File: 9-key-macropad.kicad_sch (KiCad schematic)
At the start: 0 parts

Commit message: Controller and Switch Schematic Assignments
Added the Seeed Studio XIAO-RP2040-DIP module and generic push button switch symbols to the schematic. Updated project and schematic files to include symbol definitions, global labels for keys, and wiring for a 9-key macropad design.
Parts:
- added SW1, SW2, SW3, SW4, SW5, SW6, SW7, SW8, SW9: SW_Push, Button_Switch_Keyboard:SW_Cherry_MX_1.00u_Plate, symbol Switch:SW_Push
- added U1: XIAO-RP2040-DIP, Module:MOUDLE14P-XIAO-DIP-SMD, symbol Seeed_Studio_XIAO_Series:XIAO-RP2040-DIP
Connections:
- new net GNDD: SW1.2, SW2.2, SW3.2, SW4.2, SW5.2, SW6.2, SW7.2, SW8.2, SW9.2
- new net KEY1: SW1.1, U1.1 (GPIO26/ADC0/A0)
- new net KEY2: SW2.1, U1.2 (GPIO27/ADC1/A1)
- new net KEY3: SW3.1, U1.3 (GPIO28/ADC2/A2)
- new net KEY4: SW4.1, U1.4 (GPIO29/ADC3/A3)
- new net KEY5: SW5.1, U1.5 (GPIO6/SDA)
- new net KEY6: SW6.1, U1.6 (GPIO7/SCL)
- new net KEY7: SW7.1, U1.8 (GPIO1/RX)
- new net KEY8: SW8.1, U1.9 (GPIO2/SCK)
- new net KEY9: SW9.1, U1.10 (GPIO4/MISO)
- new net NEOPIX: U1.7 (GPIO0/TX)

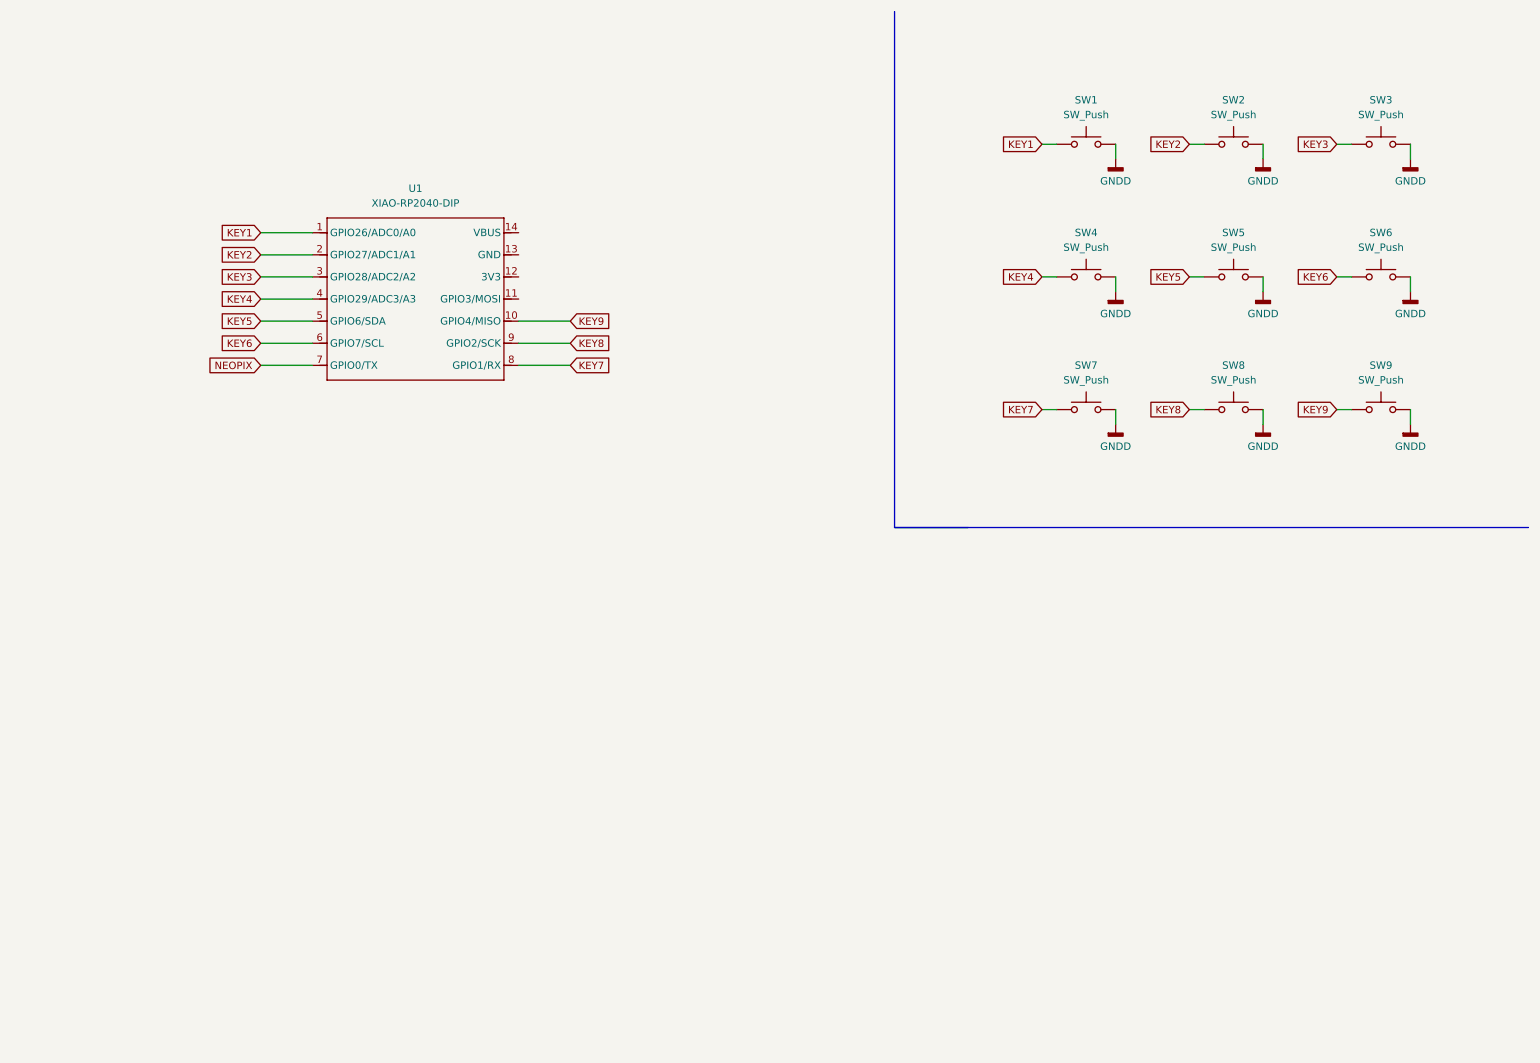
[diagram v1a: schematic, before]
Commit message: Add Step-Up library and update PCB + SCM
Added SN74AHCT1G125DBVR symbol, footprint, STEP model, and documentation to the libraries directory. Updated 9-key-macropad PCB, schematic, and project files to include new components and connections. Modified footprint and symbol library tables to reference the new library.
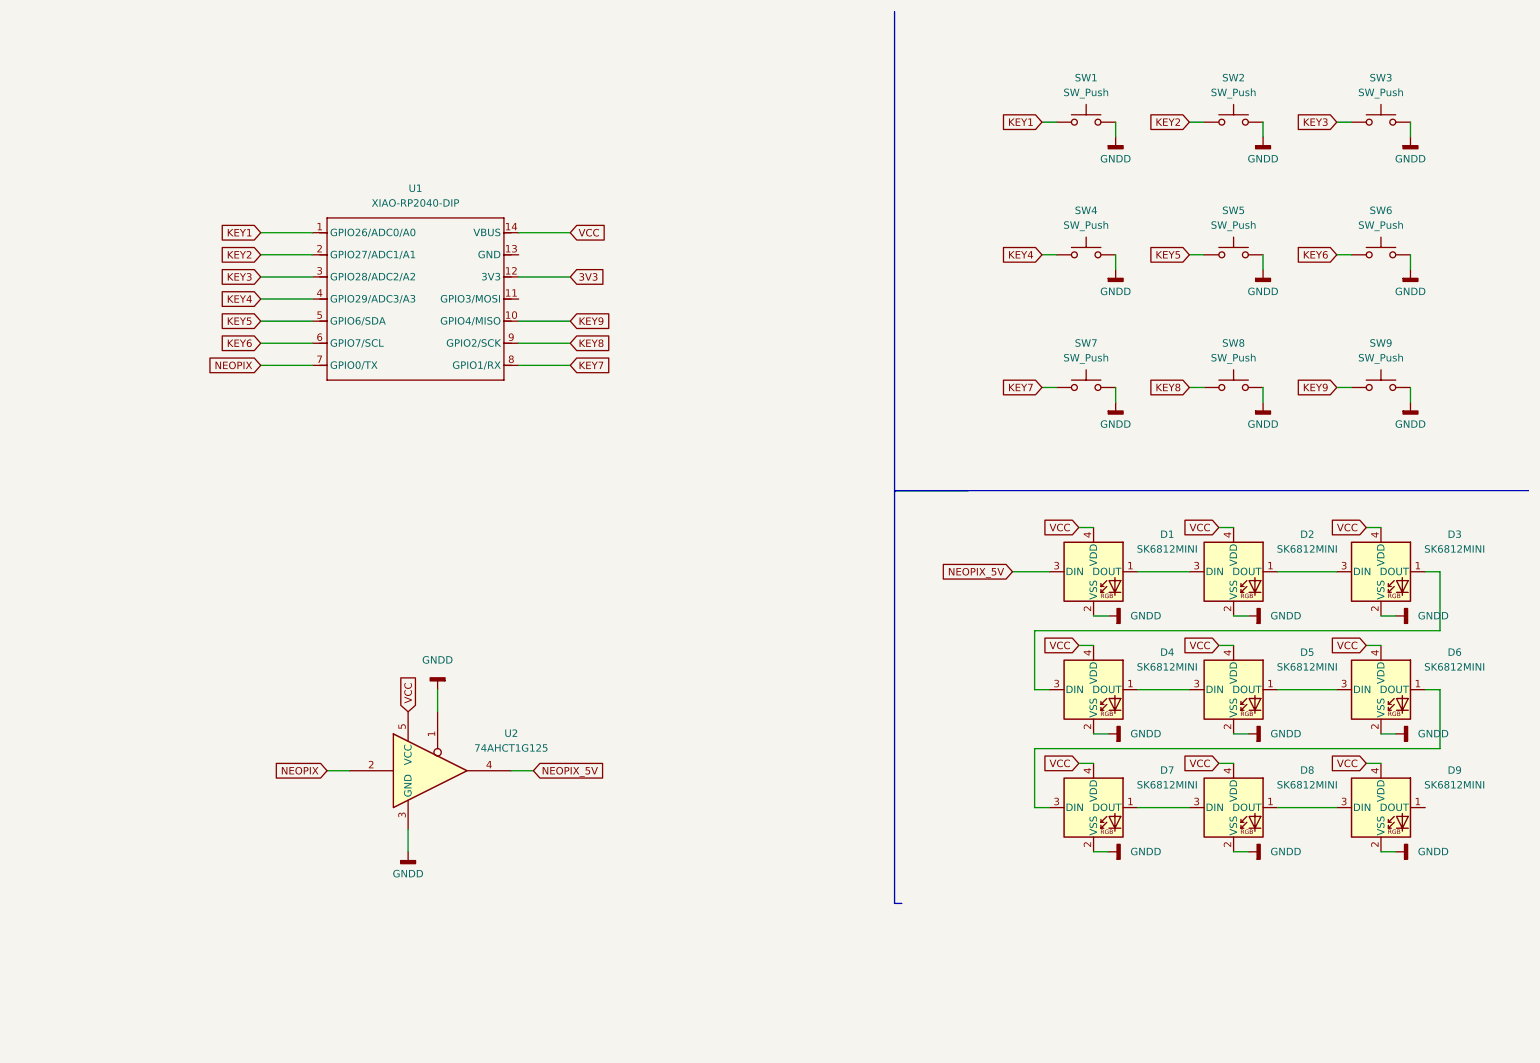
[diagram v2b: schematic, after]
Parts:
- added D1, D2, D3, D4, D5, D6, D7, D8, D9: SK6812MINI, LED_SMD:LED_SK6812MINI_PLCC4_3.5x3.5mm_P1.75mm, symbol LED:SK6812MINI
- added U2: 74AHCT1G125, SN74AHCT1G125DBVR:SOT95P280X145-5N, symbol 74xGxx:74AHCT1G125
- U1: footprint Module:MOUDLE14P-XIAO-DIP-SMD -> Seeed Studio XIAO Series Library:XIAO-RP2040-DIP
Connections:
- net GNDD: now also D1.2 (VSS), D2.2 (VSS), D3.2 (VSS), D4.2 (VSS), D5.2 (VSS), D6.2 (VSS), D7.2 (VSS), D8.2 (VSS), D9.2 (VSS), U2.1, U2.3 (GND)
- net NEOPIX: now also U2.2
- net 3V3: now reaches U1.12 (3V3)
- net VCC: now reaches U1.14 (VBUS)
- net VCC: now also D1.4 (VDD), D2.4 (VDD), D3.4 (VDD), D4.4 (VDD), D5.4 (VDD), D6.4 (VDD), D7.4 (VDD), D8.4 (VDD), D9.4 (VDD), U2.5 (VCC)
- new net: D6.1 (DOUT), D7.3 (DIN)
- new net: D5.1 (DOUT), D6.3 (DIN)
- new net: D8.1 (DOUT), D9.3 (DIN)
- new net: D7.1 (DOUT), D8.3 (DIN)
- new net: D4.1 (DOUT), D5.3 (DIN)
- new net: D3.1 (DOUT), D4.3 (DIN)
- new net: D2.1 (DOUT), D3.3 (DIN)
- new net: D1.1 (DOUT), D2.3 (DIN)
- new net NEOPIX_5V: D1.3 (DIN), U2.4
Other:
- moved on the sheet: SW1, SW2, SW3, SW4, SW5, SW6, SW7, SW8, SW9

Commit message: Rearrange key switches and LEDs, update net assignments
Moved key switches and SK6812MINI LEDs to new positions for improved layout. Updated net assignments for GPIO pins to match new key mapping and corrected NEOPIX and unconnected net references. Adjusted footprint locations for U1 and U2 to align with the new design.
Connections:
- net GNDD: now also U1.13 (GND)
- net KEY1: now also U1.10 (GPIO4/MISO); no longer U1.1 (GPIO26/ADC0/A0)
- net KEY2: now also U1.7 (GPIO0/TX); no longer U1.2 (GPIO27/ADC1/A1)
- net KEY3: now also U1.2 (GPIO27/ADC1/A1); no longer U1.3 (GPIO28/ADC2/A2)
- net KEY4: now also U1.9 (GPIO2/SCK); no longer U1.4 (GPIO29/ADC3/A3)
- net KEY5: now also U1.6 (GPIO7/SCL); no longer U1.5 (GPIO6/SDA)
- net KEY6: now also U1.3 (GPIO28/ADC2/A2); no longer U1.6 (GPIO7/SCL)
- net KEY8: now also U1.5 (GPIO6/SDA); no longer U1.9 (GPIO2/SCK)
- net KEY9: now also U1.4 (GPIO29/ADC3/A3); no longer U1.10 (GPIO4/MISO)
- net NEOPIX: now also U1.11 (GPIO3/MOSI); no longer U1.7 (GPIO0/TX)

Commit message: Continued Board Development
Reworked Schematic for better trace layout and started adding traces to PCB design
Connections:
- net KEY2: now also U1.9 (GPIO2/SCK); no longer U1.7 (GPIO0/TX)
- net KEY3: now also U1.5 (GPIO6/SDA); no longer U1.2 (GPIO27/ADC1/A1)
- net KEY4: now also U1.8 (GPIO1/RX); no longer U1.9 (GPIO2/SCK)
- net KEY7: no longer U1.8 (GPIO1/RX)
- net KEY8: now also U1.2 (GPIO27/ADC1/A1); no longer U1.5 (GPIO6/SDA)
- net at D6.1 (DOUT): now also D5.3 (DIN); no longer D7.3 (DIN)
- net at D6.3 (DIN): now also D3.1 (DOUT); no longer D5.1 (DOUT)
- net at D4.1 (DOUT): now also D7.3 (DIN); no longer D5.3 (DIN)
- net at D4.3 (DIN): now also D5.1 (DOUT); no longer D3.1 (DOUT)
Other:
- moved on the sheet: D4, D5, D6

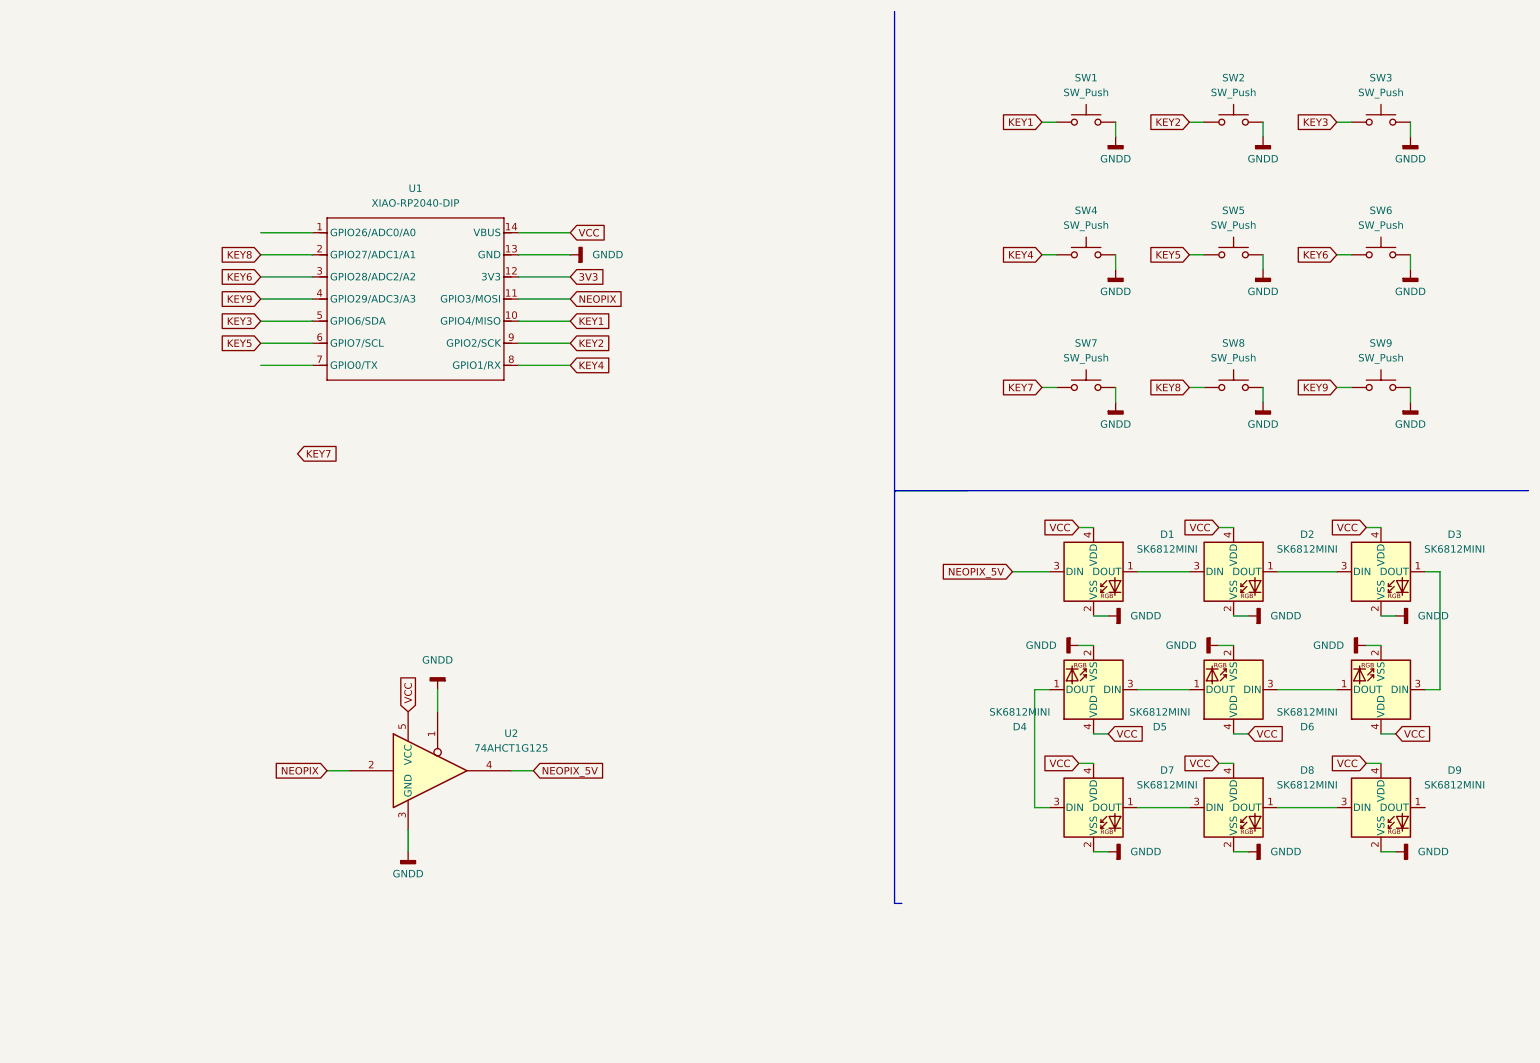
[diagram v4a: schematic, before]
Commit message: Update net assignments and LED footprints
Reorganized net numbers and names for clarity and consistency, updated LED SK6812MINI footprints and pad orientations, and corrected net connections for keys and LEDs. These changes improve schematic and PCB alignment and resolve mismatches in net assignments.
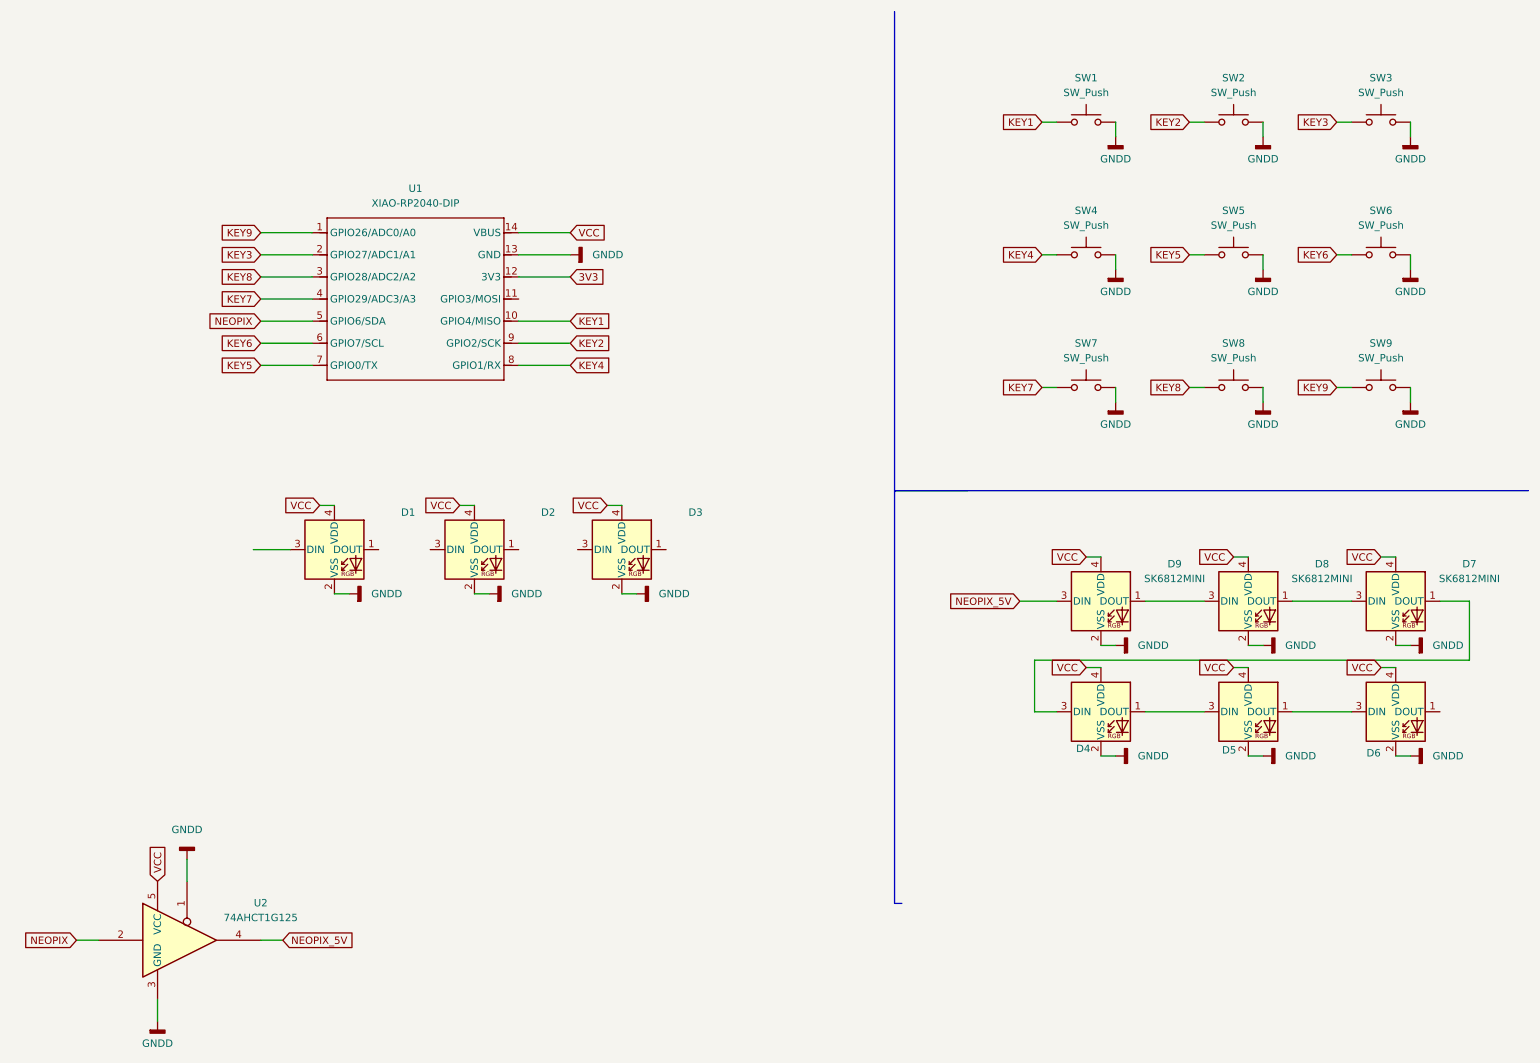
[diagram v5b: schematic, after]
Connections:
- net KEY3: now also U1.2 (GPIO27/ADC1/A1); no longer U1.5 (GPIO6/SDA)
- net KEY5: now also U1.7 (GPIO0/TX); no longer U1.6 (GPIO7/SCL)
- net KEY6: now also U1.6 (GPIO7/SCL); no longer U1.3 (GPIO28/ADC2/A2)
- net KEY7: now also U1.4 (GPIO29/ADC3/A3)
- net KEY8: now also U1.3 (GPIO28/ADC2/A2); no longer U1.2 (GPIO27/ADC1/A1)
- net KEY9: now also U1.1 (GPIO26/ADC0/A0); no longer U1.4 (GPIO29/ADC3/A3)
- net NEOPIX: now also U1.5 (GPIO6/SDA); no longer U1.11 (GPIO3/MOSI)
- net NEOPIX_5V: now also D9.3 (DIN); no longer D1.3 (DIN)
- net at D6.1 (DOUT): no longer D5.3 (DIN)
- net at D6.3 (DIN): now also D5.1 (DOUT); no longer D3.1 (DOUT)
- net at D8.1 (DOUT): now also D7.3 (DIN); no longer D9.3 (DIN)
- net at D8.3 (DIN): now also D9.1 (DOUT); no longer D7.1 (DOUT)
- net at D4.1 (DOUT): now also D5.3 (DIN); no longer D7.3 (DIN)
- net at D4.3 (DIN): now also D7.1 (DOUT); no longer D5.1 (DOUT)
- net at D3.3 (DIN): no longer D2.1 (DOUT)
- net at D2.3 (DIN): no longer D1.1 (DOUT)
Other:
- moved on the sheet: D1, D2, D3, D4, D5, D6, D7, D8, D9, U2

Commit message: PCB and schematic design complete pending review
Completed the design for the PCB and Schematic.

Holding off having it printed until I can find a professional to review it.
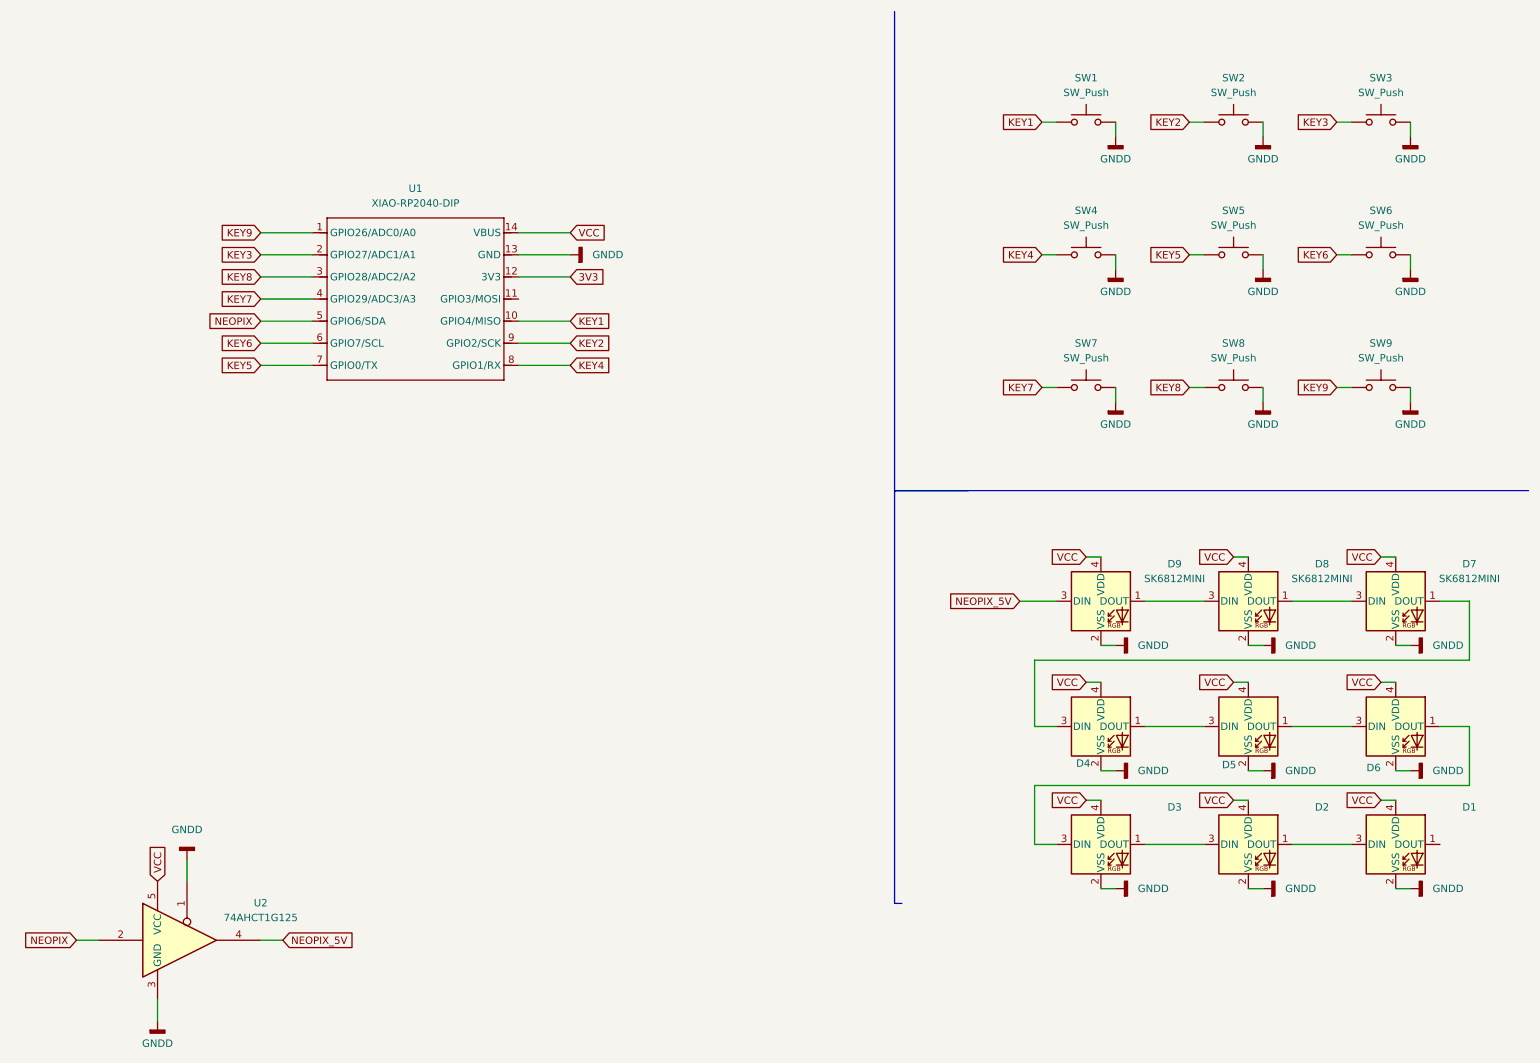
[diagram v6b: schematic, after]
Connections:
- net at D6.1 (DOUT): now also D3.3 (DIN)
- net at D3.1 (DOUT): now also D2.3 (DIN)
- net at D2.1 (DOUT): now also D1.3 (DIN)
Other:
- moved on the sheet: D1, D2, D3, D4, D5, D6
